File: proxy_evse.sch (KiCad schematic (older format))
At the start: 6 parts, among them Q401 AO3400A, Q402 AO3400A

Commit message: Add files via upload
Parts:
- Q401, Q402: footprint (none) -> Package_TO_SOT_SMD:SOT-23
- R401, R402, R403, R404: footprint (none) -> Resistor_SMD:R_0402_1005Metric
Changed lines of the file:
@@
 F 0 "R403" H 3368 3496 50  0000 L CNN
 F 1 "150" H 3368 3405 50  0000 L CNN
-F 2 "" H 3300 3450 50  0001 C CNN
+F 2 "Resistor_SMD:R_0402_1005Metric" H 3300 3450 50  0001 C CNN
 F 3 "~" H 3300 3450 50  0001 C CNN
 	1    3300 3450
@@
 F 0 "R404" H 3368 3946 50  0000 L CNN
 F 1 "330" H 3368 3855 50  0000 L CNN
-F 2 "" H 3300 3900 50  0001 C CNN
+F 2 "Resistor_SMD:R_0402_1005Metric" H 3300 3900 50  0001 C CNN
 F 3 "~" H 3300 3900 50  0001 C CNN
 	1    3300 3900
@@
 F 0 "Q401" H 2705 3896 50  0000 L CNN
 F 1 "AO3400A" H 2705 3805 50  0000 L CNN
-F 2 "" H 2700 3950 50  0001 C CNN
+F 2 "Package_TO_SOT_SMD:SOT-23" H 2700 3950 50  0001 C CNN
 F 3 "~" H 2500 3850 50  0001 C CNN
 	1    2500 3850
@@
 F 0 "Q402" H 2800 4800 50  0000 L CNN
 F 1 "AO3400A" H 2800 4700 50  0000 L CNN
-F 2 "" H 3400 4750 50  0001 C CNN
+F 2 "Package_TO_SOT_SMD:SOT-23" H 3400 4750 50  0001 C CNN
 F 3 "~" H 3200 4650 50  0001 C CNN
 	1    3200 4650
@@
 F 0 "R401" H 2318 4096 50  0000 L CNN
 F 1 "10k" H 2318 4005 50  0000 L CNN
-F 2 "" H 2250 4050 50  0001 C CNN
+F 2 "Resistor_SMD:R_0402_1005Metric" H 2250 4050 50  0001 C CNN
 F 3 "~" H 2250 4050 50  0001 C CNN
 	1    2250 4050
@@
 F 0 "R402" H 2968 4896 50  0000 L CNN
 F 1 "10k" H 2968 4805 50  0000 L CNN
-F 2 "" H 2900 4850 50  0001 C CNN
+F 2 "Resistor_SMD:R_0402_1005Metric" H 2900 4850 50  0001 C CNN
 F 3 "~" H 2900 4850 50  0001 C CNN
 	1    2900 4850

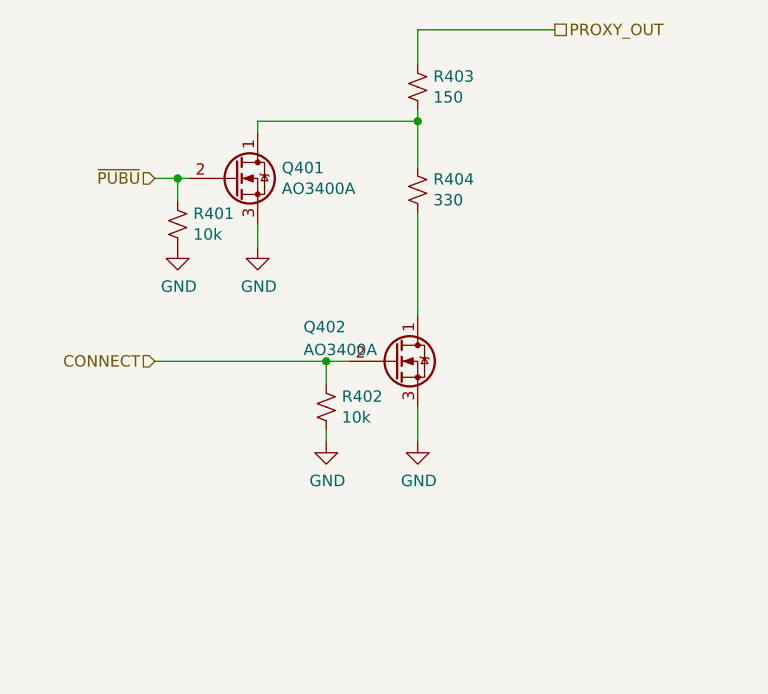
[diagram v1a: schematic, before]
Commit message: Submited for production & smt assembly
v0.01
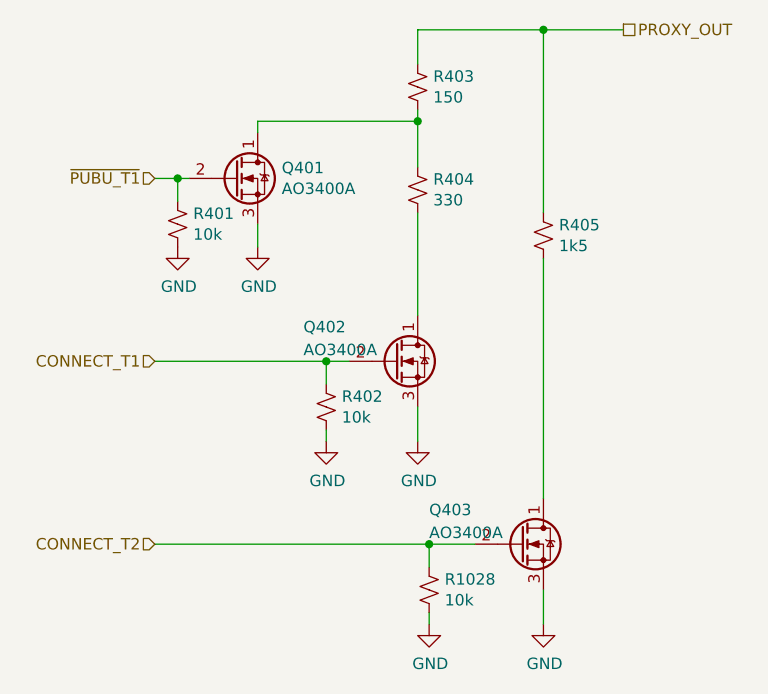
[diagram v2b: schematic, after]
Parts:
- added Q403: AO3400A, Package_TO_SOT_SMD:SOT-23, symbol Device:Q_NMOS_DGS
- added R1028: 10k, Resistor_SMD:R_0402_1005Metric, symbol Device:R_Small_US
- added R405: 1k5, Resistor_SMD:R_0402_1005Metric, symbol Device:R_Small_US
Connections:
- net GND: now also Q403.3 (S), R1028.2
- net PROXY_OUT: now also R405.1
- net CONNECT renamed CONNECT_T1
- net ~PUBU renamed ~PUBU_T1
- new net: Q403.1 (D), R405.2
- new net CONNECT_T2: Q403.2 (G), R1028.1
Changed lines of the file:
@@
 $Descr A4 11693 8268
 encoding utf-8
-Sheet 4 10
+Sheet 10 10
 Title ""
 Date ""
@@
 $EndDescr
 Text HLabel 2150 3850 0    50   Input ~ 0
-~PUBU
+~PUBU_T1
 $Comp
 L Device:R_Small_US R403
@@
 	3300 3350 3300 3200
 Wire Wire Line
-	3300 3200 3900 3200
-Text HLabel 3900 3200 2    50   UnSpc ~ 0
+	3300 3200 3850 3200
+Text HLabel 4200 3200 2    50   UnSpc ~ 0
 PROXY_OUT
 $Comp
@@
 	3000 4650 2900 4650
 Text HLabel 2150 4650 0    50   Input ~ 0
-CONNECT
+CONNECT_T1
 $Comp
 L power:GND #PWR0404
@@
 	1    0    0    -1
 $EndComp
+$Comp
+L Device:R_Small_US R405
+U 1 1 5F08241B
+P 3850 4100
+F 0 "R405" H 3918 4146 50  0000 L CNN
+F 1 "1k5" H 3918 4055 50  0000 L CNN
+F 2 "Resistor_SMD:R_0402_1005Metric" H 3850 4100 50  0001 C CNN
+F 3 "~" H 3850 4100 50  0001 C CNN
+	1    3850 4100
+	1    0    0    -1
+$EndComp
+Wire Wire Line
+	3850 4000 3850 3200
+Connection ~ 3850 3200
+Wire Wire Line
+	3850 3200 4200 3200
+$Comp
+L Device:Q_NMOS_DGS Q403
+U 1 1 5F082B77
+P 3750 5450
+F 0 "Q403" H 3350 5600 50  0000 L CNN
+F 1 "AO3400A" H 3350 5500 50  0000 L CNN
+F 2 "Package_TO_SOT_SMD:SOT-23" H 3950 5550 50  0001 C CNN
+F 3 "~" H 3750 5450 50  0001 C CNN
+	1    3750 5450
+	1    0    0    -1
+$EndComp
+Wire Wire Line
+	3850 5250 3850 4200
+Wire Wire Line
+	3850 5650 3850 5800
+$Comp
+L power:GND #PWR0405
+U 1 1 5F083E5B
+P 3850 5800
+F 0 "#PWR0405" H 3850 5550 50  0001 C CNN
+F 1 "GND" H 3855 5627 50  0000 C CNN
+F 2 "" H 3850 5800 50  0001 C CNN
+F 3 "" H 3850 5800 50  0001 C CNN
+	1    3850 5800
+	1    0    0    -1
+$EndComp
+Wire Wire Line
+	3550 5450 3350 5450
+Text HLabel 2150 5450 0    50   Input ~ 0
+CONNECT_T2
+$Comp
+L Device:R_Small_US R1028
+U 1 1 5F08538E
+P 3350 5650
+F 0 "R1028" H 3418 5696 50  0000 L CNN
+F 1 "10k" H 3418 5605 50  0000 L CNN
+F 2 "Resistor_SMD:R_0402_1005Metric" H 3350 5650 50  0001 C CNN
+F 3 "~" H 3350 5650 50  0001 C CNN
+	1    3350 5650
+	1    0    0    -1
+$EndComp
+Wire Wire Line
+	3350 5550 3350 5450
+Connection ~ 3350 5450
+Wire Wire Line
+	3350 5450 2150 5450
+$Comp
+L power:GND #PWR0123
+U 1 1 5F085A65
+P 3350 5800
+F 0 "#PWR0123" H 3350 5550 50  0001 C CNN
+F 1 "GND" H 3355 5627 50  0000 C CNN
+F 2 "" H 3350 5800 50  0001 C CNN
+F 3 "" H 3350 5800 50  0001 C CNN
+	1    3350 5800
+	1    0    0    -1
+$EndComp
+Wire Wire Line
+	3350 5800 3350 5750
 $EndSCHEMATC
